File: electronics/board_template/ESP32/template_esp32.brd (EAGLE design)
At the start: 48 x 48 mm, 51 parts, among them IC1 ESP-WROOM-32D, IC2 CP2104-F03-GMR, IC3 NCP1117ST50T3G, IC4 LMV358IDGKRG4, IC5 NCP1117ST33T3G, J1 GROVE_CONNECTOR2.0_1X4, J2 GROVE_CONNECTOR2.0_1X4, J4 10129383-912001ALF, J5 10129383-912001ALF, Q1 FDN340P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

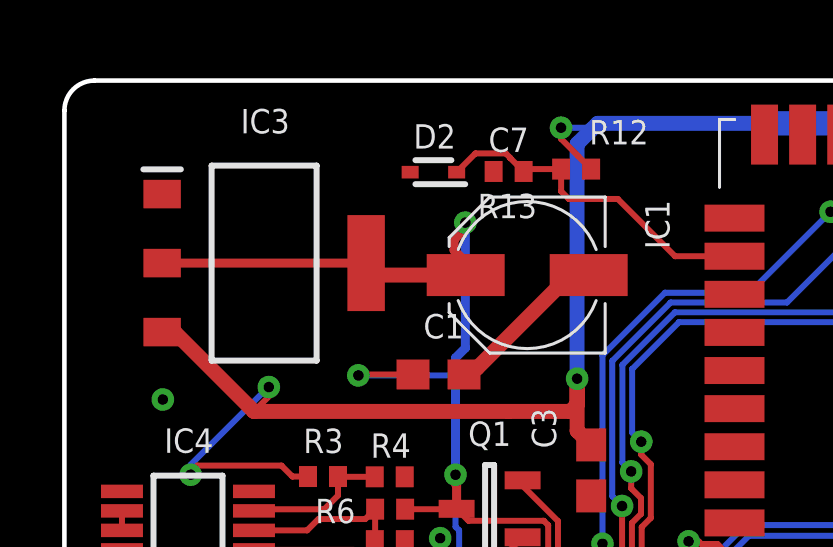
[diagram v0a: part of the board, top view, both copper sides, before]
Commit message: Logo hinzugefügt
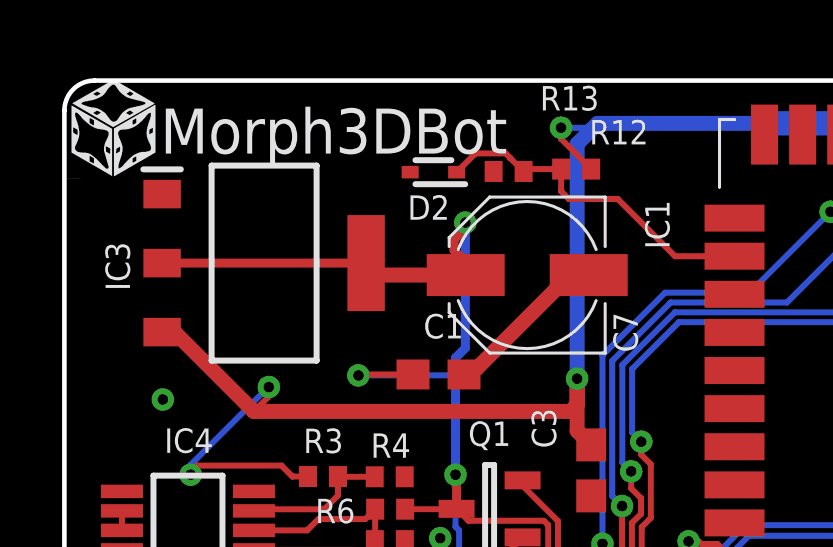
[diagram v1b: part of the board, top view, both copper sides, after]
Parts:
- added U$1: LOGO_MORPHBOT3MM, topo-eng:LOGO_MOPRHBOT_3MM
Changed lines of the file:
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@@
 <layer number="104" name="Name" color="7" fill="1" visible="no" active="yes"/>
 <layer number="116" name="Patch_BOT" color="9" fill="4" visible="no" active="yes"/>
+<layer number="120" name="brd_placement_notes" color="7" fill="1" visible="yes" active="yes"/>
 <layer number="121" name="_tsilk" color="7" fill="1" visible="no" active="yes"/>
 <layer number="122" name="_bsilk" color="7" fill="1" visible="no" active="yes"/>
+<layer number="144" name="DrillLegend" color="7" fill="1" visible="yes" active="yes"/>
+<layer number="145" name="DrillLegend_01-16" color="7" fill="1" visible="yes" active="yes"/>
+<layer number="146" name="DrillLegend_01-20" color="7" fill="1" visible="yes" active="yes"/>
 <layer number="151" name="HeatSink" color="14" fill="1" visible="no" active="no"/>
+<layer number="198" name="BMP198" color="7" fill="1" visible="yes" active="yes"/>
+<layer number="199" name="Contour" color="7" fill="1" visible="yes" active="yes"/>
 <layer number="200" name="200bmp" color="1" fill="10" visible="no" active="no"/>
 <layer number="201" name="201bmp" color="2" fill="1" visible="no" active="no"/>
@@
 <layer number="207" name="207bmp" color="15" fill="10" visible="no" active="no"/>
 <layer number="208" name="208bmp" color="9" fill="10" visible="no" active="yes"/>
+<layer number="209" name="Route9Document" color="7" fill="1" visible="yes" active="yes"/>
+<layer number="210" name="Route10Document" color="7" fill="1" visible="yes" active="yes"/>
+<layer number="211" name="Route11Document" color="7" fill="1" visible="yes" active="yes"/>
+<layer number="212" name="Route12Document" color="7" fill="1" visible="yes" active="yes"/>
+<layer number="213" name="Route13Document" color="7" fill="1" visible="yes" active="yes"/>
+<layer number="214" name="Route14Document" color="7" fill="1" visible="yes" active="yes"/>
+<layer number="215" name="Route15Document" color="7" fill="1" visible="yes" active="yes"/>
+<layer number="216" name="BottomDocument" color="7" fill="1" visible="yes" active="yes"/>
+<layer number="220" name="DimensionDocument" color="7" fill="1" visible="yes" active="yes"/>
+<layer number="221" name="tPlaceDocument" color="7" fill="1" visible="yes" active="yes"/>
+<layer number="222" name="bPlaceDocument" color="7" fill="1" visible="yes" active="yes"/>
+<layer number="225" name="tNamesDocument" color="7" fill="1" visible="yes" active="yes"/>
+<layer number="226" name="bNamesDocument" color="7" fill="1" visible="yes" active="yes"/>
+<layer number="227" name="tValuesDocument" color="7" fill="1" visible="yes" active="yes"/>
+<layer number="228" name="bValuesDocument" color="7" fill="1" visible="yes" active="yes"/>
+<layer number="229" name="tStopDocument" color="7" fill="1" visible="yes" active="yes"/>
+<layer number="230" name="bStopDocument" color="7" fill="1" visible="yes" active="yes"/>
+<layer number="231" name="tCreamDocument" color="7" fill="1" visible="yes" active="yes"/>
+<layer number="232" name="bCreamDocument" color="7" fill="1" visible="yes" active="yes"/>
+<layer number="233" name="tFinishDocument" color="7" fill="1" visible="yes" active="yes"/>
+<layer number="234" name="bFinishDocument" color="7" fill="1" visible="yes" active="yes"/>
+<layer number="235" name="tGlueDocument" color="7" fill="1" visible="yes" active="yes"/>
+<layer number="236" name="bGlueDocument" color="7" fill="1" visible="yes" active="yes"/>
+<layer number="244" name="DrillsDocument" color="7" fill="1" visible="yes" active="yes"/>
+<layer number="245" name="HolesDocument" color="7" fill="1" visible="yes" active="yes"/>
+<layer number="246" name="MillingDocument" color="7" fill="1" visible="yes" active="yes"/>
+<layer number="247" name="MeasuresDocument" color="7" fill="1" visible="yes" active="yes"/>
 <layer number="250" name="Descript" color="3" fill="1" visible="no" active="no"/>
 <layer number="251" name="SMDround" color="12" fill="11" visible="no" active="no"/>
@@
 <attribute name="MOUSER_PART_NUMBER" value="863-NCP1117ST50T3G" x="6.65716875" y="41.91548125" size="1.778" layer="27" display="off"/>
 <attribute name="MOUSER_PRICE-STOCK" value="https://www.mouser.co.uk/ProductDetail/ON-Semiconductor/NCP1117ST50T3G?qs=Gev%252BmEvV0ib6dijy6U0dhQ%3D%3D" x="6.65716875" y="41.91548125" size="1.778" layer="27" display="off"/>
-<attribute name="NAME" x="6.692225" y="46.64605" size="0.8128" layer="25" rot="R180" align="center"/>
+<attribute name="NAME" x="1.77896875" y="41.80615625" size="0.8128" layer="25" rot="R270" align="center"/>
 <attribute name="VALUE" x="6.65716875" y="41.91548125" size="1.27" layer="27" align="center"/>
 </element>
 <element name="C7" library="rcl" library_urn="urn:adsk.eagle:library:334" package="PANASONIC_C" package3d_urn="urn:adsk.eagle:package:23422/2" value="ST(Semtech) CK1C470M-CRD54 - 47uF" x="15.426159375" y="41.516775" smashed="yes" rot="R180">
-<attribute name="NAME" x="15.476109375" y="46.43353125" size="0.8128" layer="25" rot="R180"/>
+<attribute name="NAME" x="18.302871875" y="40.276578125" size="0.8128" layer="25" rot="R270"/>
 <attribute name="POPULARITY" value="4" x="15.426159375" y="41.516775" size="1.778" layer="27" rot="R180" display="off"/>
 <attribute name="SPICEPREFIX" value="C" x="15.426159375" y="41.516775" size="1.778" layer="27" rot="R180" display="off"/>
@@
 </element>
 <element name="R13" library="rcl" library_urn="urn:adsk.eagle:library:334" package="R0402" package3d_urn="urn:adsk.eagle:package:23547/3" value="Uniroyal Elec 0402WGF3900TCE - 390R" x="14.8081" y="44.9694375" smashed="yes">
-<attribute name="NAME" x="13.776415625" y="43.4124375" size="0.8128" layer="25"/>
+<attribute name="NAME" x="15.852390625" y="47.0031" size="0.8128" layer="25"/>
 <attribute name="POPULARITY" value="0" x="14.8081" y="44.9694375" size="1.778" layer="27" display="off"/>
 <attribute name="SPICEPREFIX" value="R" x="14.8081" y="44.9694375" size="1.778" layer="27" display="off"/>
@@
 <attribute name="MOUSER_PART_NUMBER" value="621-BZT52C3V3T-7" x="12.300746875" y="44.94625625" size="0.8128" layer="27" rot="R180" display="off"/>
 <attribute name="MOUSER_PRICE-STOCK" value="https://www.mouser.co.uk/ProductDetail/Diodes-Incorporated/BZT52C3V3T-7?qs=zLeapIUCO8SeTE43ANZQdw%3D%3D" x="12.300746875" y="44.94625625" size="0.8128" layer="27" rot="R180" display="off"/>
-<attribute name="NAME" x="12.340503125" y="46.13875" size="0.8128" layer="25" rot="R180" align="center"/>
+<attribute name="NAME" x="12.142790625" y="43.766934375" size="0.8128" layer="25" rot="R180" align="center"/>
 <attribute name="VALUE" x="12.300746875" y="44.94625625" size="1.27" layer="27" rot="R180" align="center"/>
 </element>
@@
 <attribute name="VALUE" x="13.968846875" y="29.92159375" size="1.27" layer="27" rot="R270"/>
 </element>
+<element name="U$1" library="topo-eng" library_urn="urn:adsk.eagle:library:6646478" package="LOGO_MOPRHBOT_3MM" value="LOGO_MORPHBOT3MM" x="0.088325" y="44.75038125" smashed="yes"/>
 </elements>
 <signals>

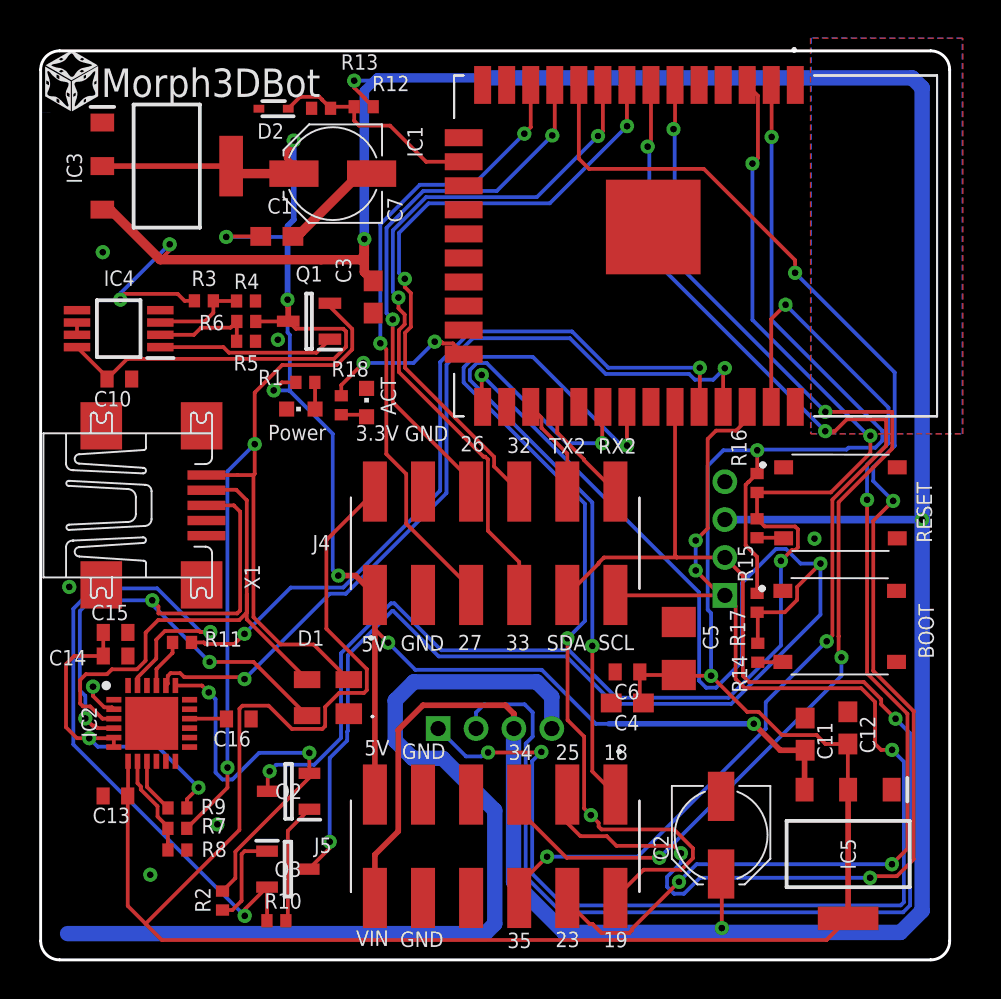
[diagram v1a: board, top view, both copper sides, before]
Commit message: Fiducials eingefügt
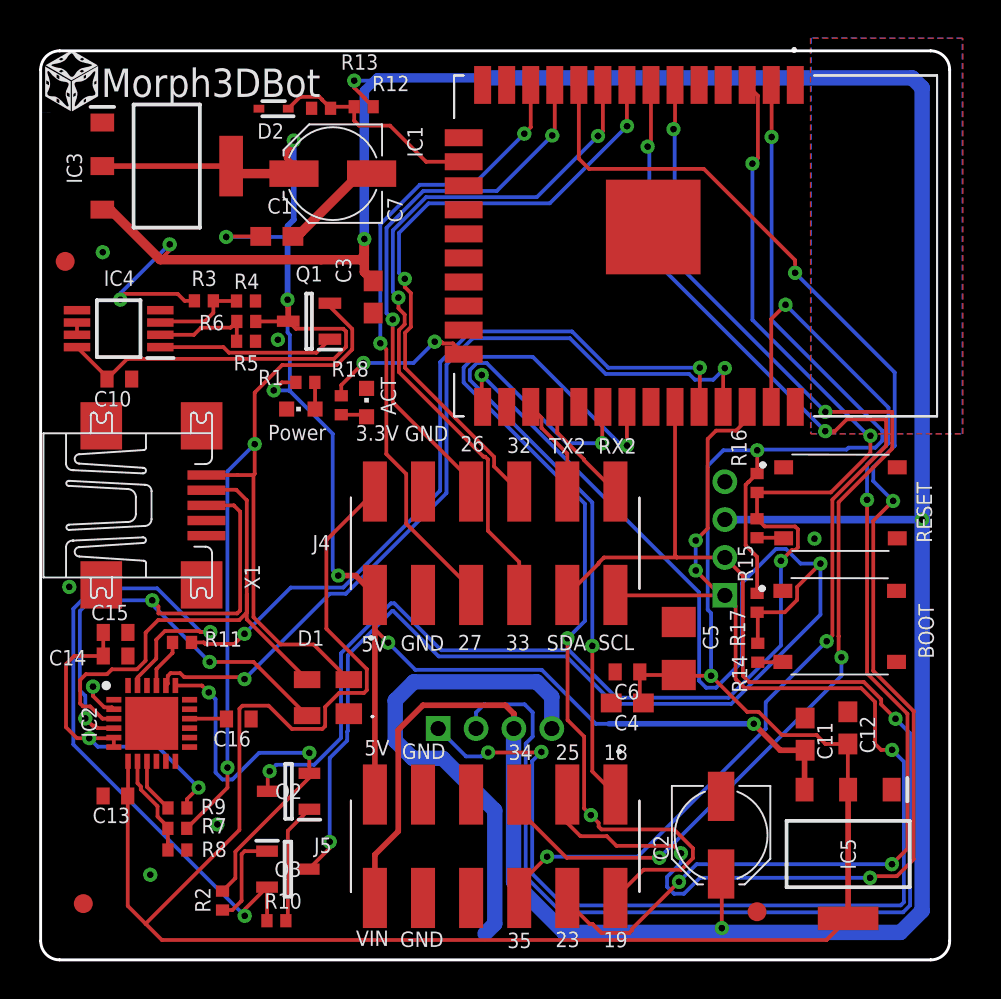
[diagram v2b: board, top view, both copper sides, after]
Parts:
- added FID1, FID2, FID3: OPEN-PNP-FIDUCIAL, topo-eng:OPEN-PNP-FIDUCIAL
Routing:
- net GND: track 55.7 -> 33.7 mm
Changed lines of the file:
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@@
 <layer number="14" name="Route14" color="22" fill="1" visible="no" active="no"/>
 <layer number="15" name="Route15" color="23" fill="1" visible="no" active="no"/>
-<layer number="16" name="Bottom" color="1" fill="1" visible="no" active="yes"/>
+<layer number="16" name="Bottom" color="1" fill="1" visible="yes" active="yes"/>
 <layer number="17" name="Pads" color="2" fill="1" visible="yes" active="yes"/>
 <layer number="18" name="Vias" color="14" fill="1" visible="yes" active="yes"/>
@@
 </element>
 <element name="U$1" library="topo-eng" library_urn="urn:adsk.eagle:library:6646478" package="LOGO_MOPRHBOT_3MM" value="LOGO_MORPHBOT3MM" x="0.088325" y="44.75038125" smashed="yes"/>
+<element name="FID1" library="topo-eng" library_urn="urn:adsk.eagle:library:6646478" package="OPEN-PNP-FIDUCIAL" value="OPEN-PNP-FIDUCIAL" x="2.252828125" y="2.971290625" smashed="yes"/>
+<element name="FID2" library="topo-eng" library_urn="urn:adsk.eagle:library:6646478" package="OPEN-PNP-FIDUCIAL" value="OPEN-PNP-FIDUCIAL" x="37.827975" y="2.543028125" smashed="yes"/>
+<element name="FID3" library="topo-eng" library_urn="urn:adsk.eagle:library:6646478" package="OPEN-PNP-FIDUCIAL" value="OPEN-PNP-FIDUCIAL" x="1.295975" y="36.88231875" smashed="yes"/>
 </elements>
 <signals>
@@
 <contactref element="C1" pad="2"/>
 <contactref element="LED1" pad="C"/>
-<wire x1="1.419528125" y1="1.3874875" x2="23.4645875" y2="1.3874875" width="0.8128" layer="16"/>
 <wire x1="23.4645875" y1="1.3874875" x2="23.977990625" y2="1.900890625" width="0.8128" layer="16"/>
 <wire x1="23.977990625" y1="1.900890625" x2="23.977990625" y2="7.8975875" width="0.8128" layer="16"/>

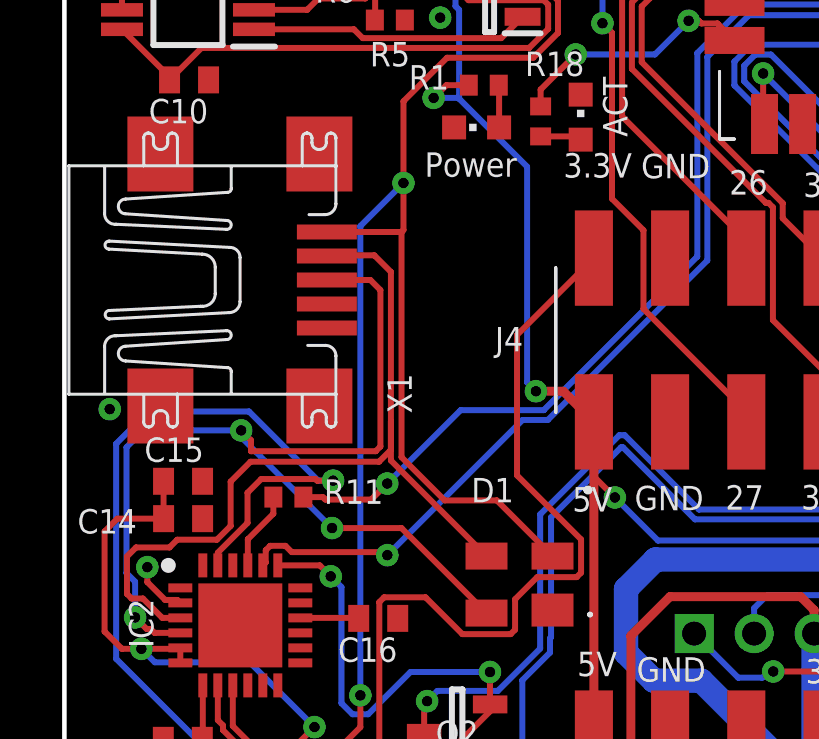
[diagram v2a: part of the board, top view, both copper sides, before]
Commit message: ESP32-Template: - USB-Datenleitungen getauscht (BugFix) 328P-Template: - USB-Datenleitungen getauscht (BugFix) - Reset-Leitung mit DTR verbunden (Zum Programieren über ARDUINO-IDE notwendig)
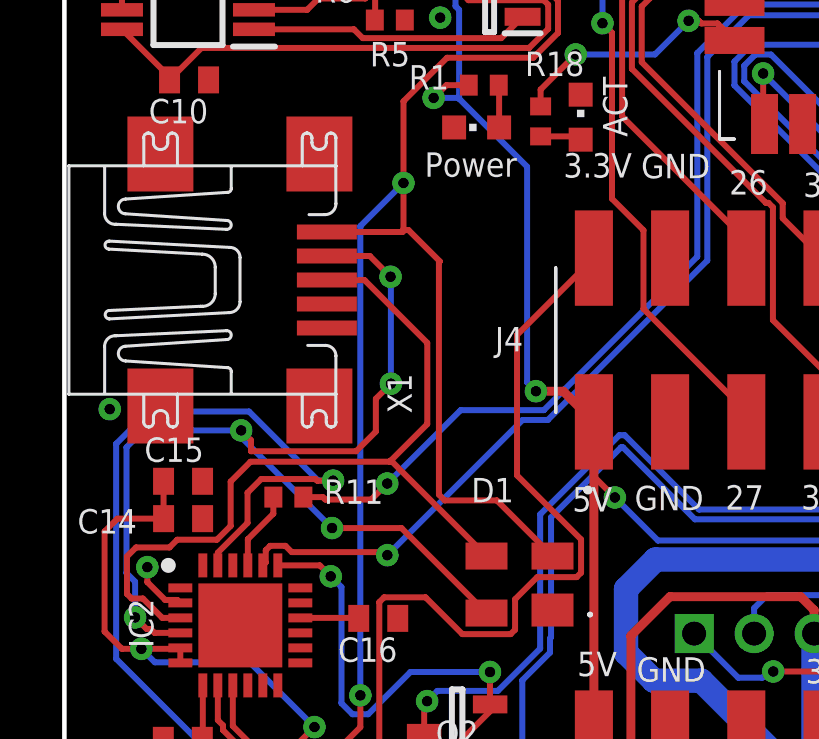
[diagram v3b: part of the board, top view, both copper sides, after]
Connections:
- net USB_DN: now also X1.2; no longer X1.3
- net USB_DP: now also X1.3; no longer X1.2
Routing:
- net USB_DP: track 28.6 -> 27.5 mm
- net USB_DN: track 34.7 -> 35.4 mm, vias 3 -> 5
